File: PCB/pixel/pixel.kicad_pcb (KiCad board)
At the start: 2 copper layers, 75 x 75 mm, 281 parts, among them CON1 BARREL_JACK, P1 CONN_01X04, U1 APA102, U10 APA102, U100 APA102, U101 APA102, U102 APA102, U103 APA102, U104 APA102, U105 APA102, U106 APA102, U107 APA102, U108 APA102, U109 APA102, U11 APA102, U110 APA102, U111 APA102, U112 APA102, U113 APA102, U114 APA102, U115 APA102, U116 APA102, U117 APA102, U118 APA102, U119 APA102, U12 APA102, U120 APA102, U121 APA102, U122 APA102, U123 APA102, U124 APA102, U125 APA102, U126 APA102, U127 APA102, U128 APA102, U129 APA102, U13 APA102, U130 APA102, U131 APA102, U132 APA102, U133 APA102, U134 APA102, U135 APA102, U136 APA102, U137 APA102, U138 APA102, U139 APA102, U14 APA102, U140 APA102, U141 APA102, U142 APA102, U143 APA102, U144 APA102, U145 APA102, U146 APA102, U147 APA102, U148 APA102, U149 APA102, U15 APA102, U150 APA102, U151 APA102, U152 APA102, U153 APA102, U154 APA102, U155 APA102, U156 APA102, U157 APA102, U158 APA102, U159 APA102, U16 APA102, U160 APA102, U161 APA102, U162 APA102, U163 APA102, U164 APA102, U165 APA102, U166 APA102, U167 APA102, U168 APA102, U169 APA102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

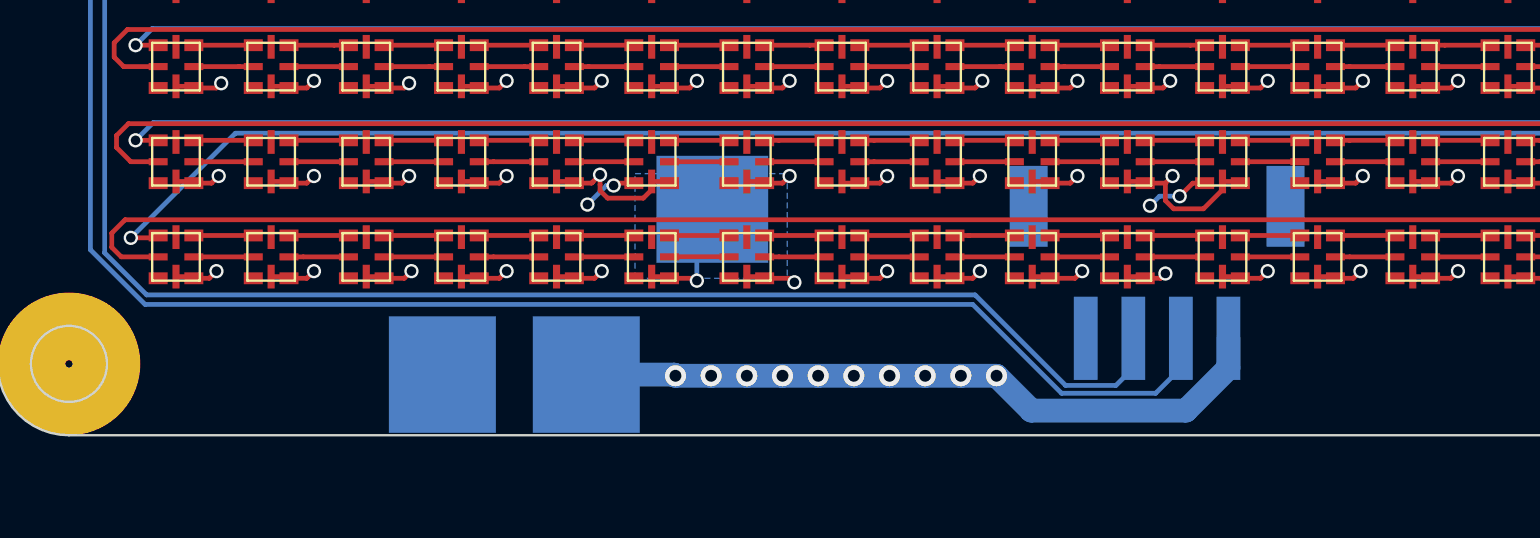
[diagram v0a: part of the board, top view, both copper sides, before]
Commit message: added fuse, fixed traces
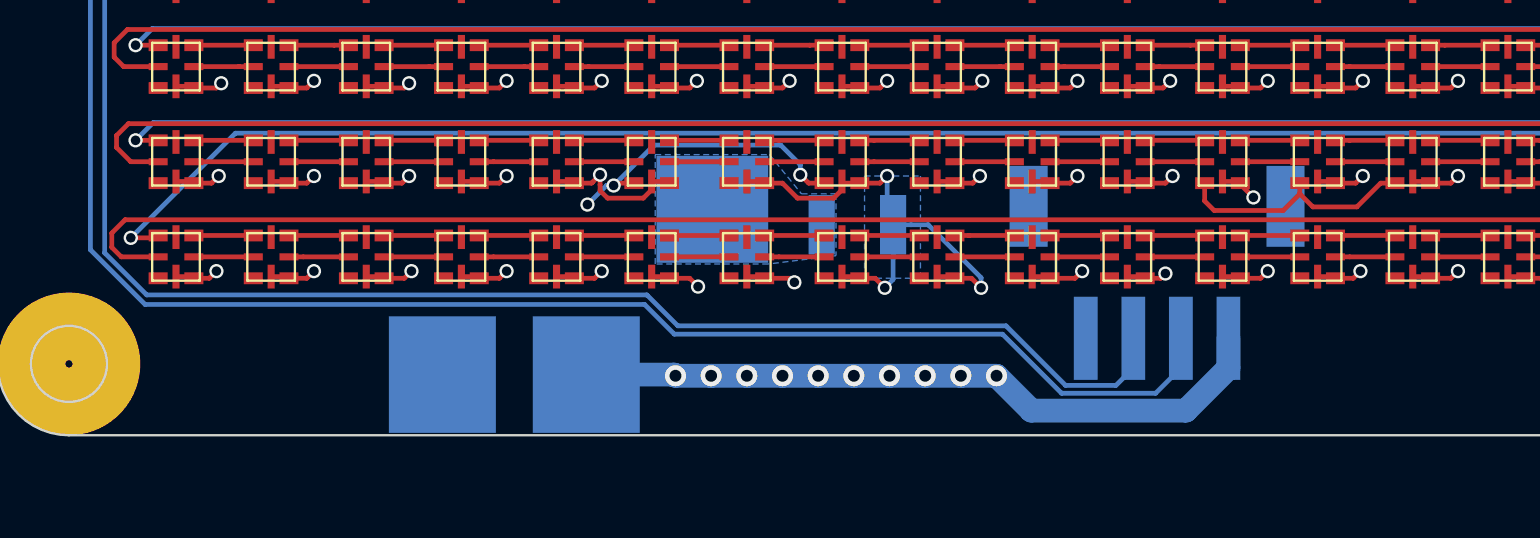
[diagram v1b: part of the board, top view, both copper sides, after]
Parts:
- added F1: 5A_Hold, idlehands_footprints:Fuse_SMD1210_Reflow, B.Cu at (133.2, 163.2)
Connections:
- CON1 pad 1: +5V -> Net-(CON1-Pad1)
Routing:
- net GND: track 123.9 -> 142.0 mm, vias 45 -> 44
- net +5V: track 531.4 -> 538.2 mm
- added copper zone on B.Cu, net Net-(CON1-Pad1)

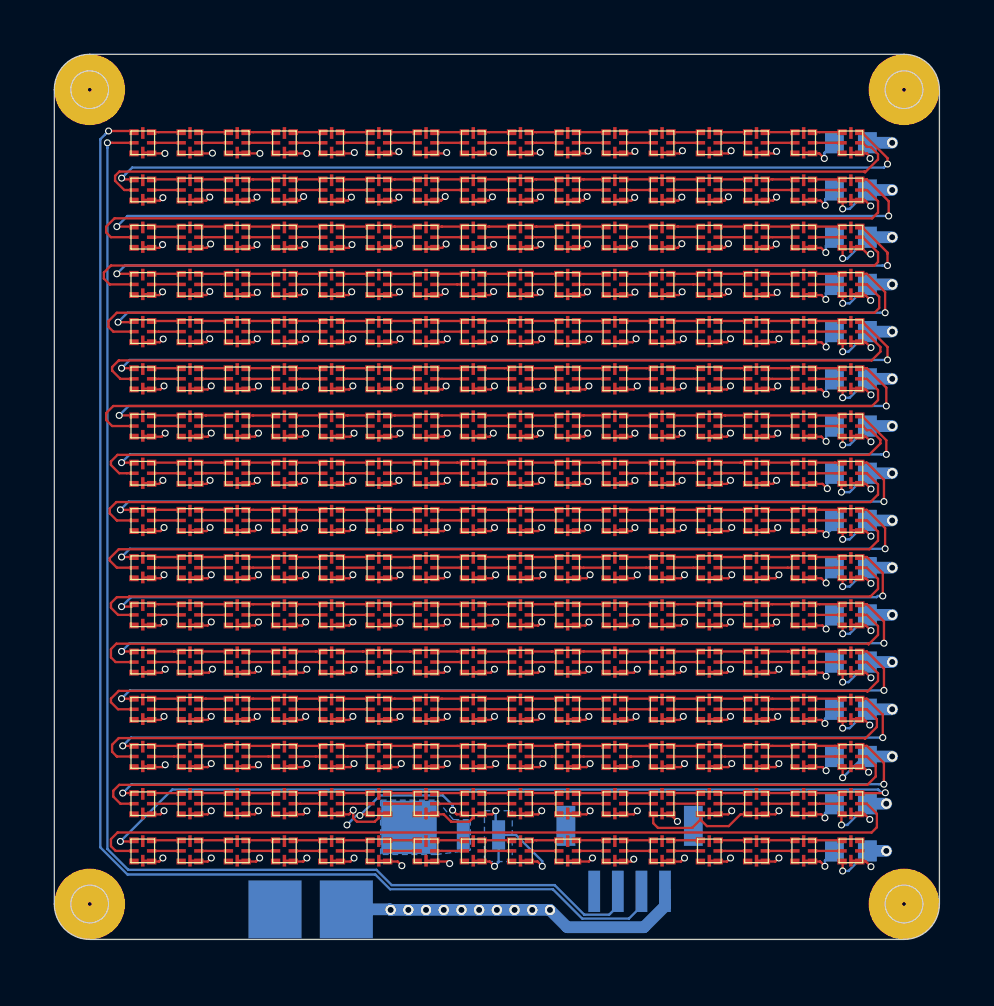
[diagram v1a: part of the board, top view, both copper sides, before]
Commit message: changed led pad layout
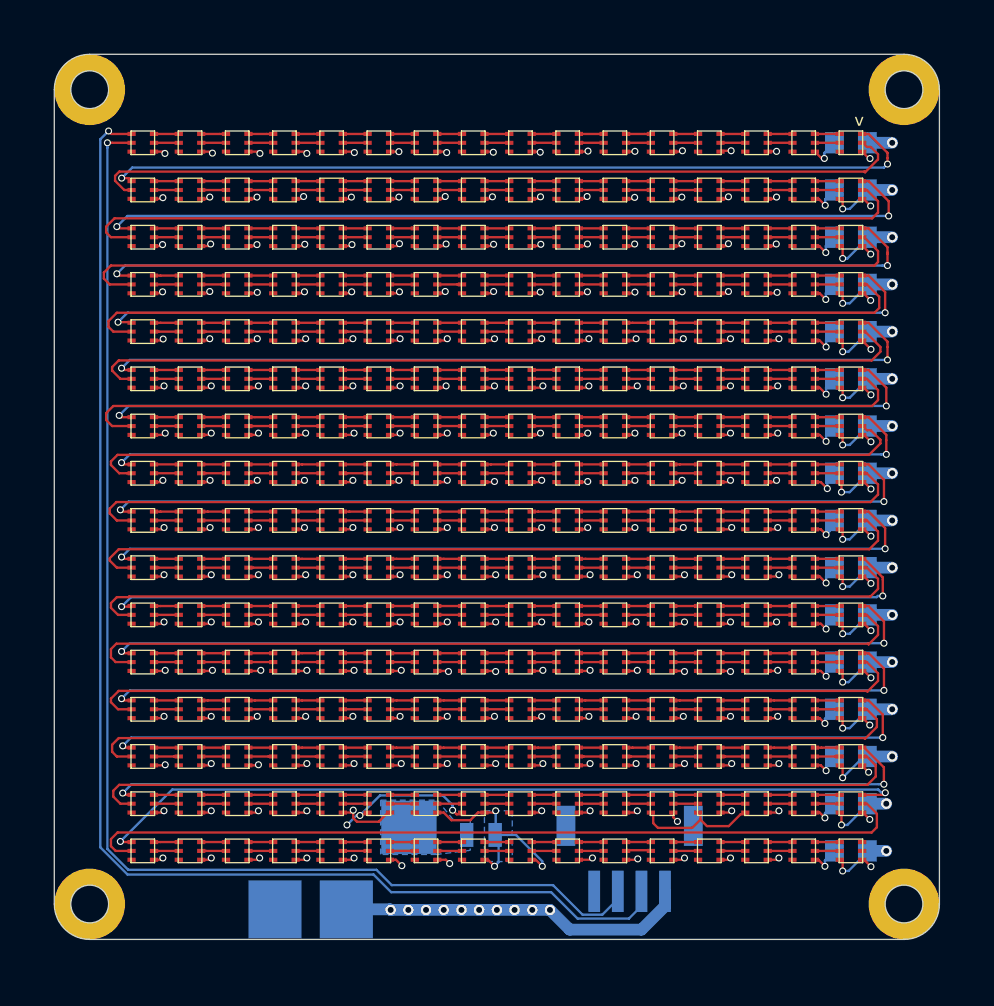
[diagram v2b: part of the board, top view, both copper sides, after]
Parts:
- F1: footprint idlehands_footprints:Fuse_SMD1210_Reflow -> Fuse_Holders_and_Fuses:Fuse_SMD1206_Reflow
- U1, U10, U100, U101, U102, U103, U104, U105, U106, U107, U108, U109, U11, U110, U111, U112, U113, U114, U115, U116, U117, U118, U119, U12, U120, U121, U122, U123, U124, U125, U126, U127, U128, U129, U13, U130, U131, U132, U133, U134, U135, U136, U137, U138, U139, U14, U140, U141, U142, U143, U144, U145, U146, U147, U148, U149, U15, U150, U151, U152, U153, U154, U155, U156, U157, U158, U159, U16, U160, U161, U162, U163, U164, U165, U166, U167, U168, U169, U17, U170, U171, U172, U173, U174, U175, U176, U177, U178, U179, U18, U180, U181, U182, U183, U184, U185, U186, U187, U188, U189, U19, U190, U191, U192, U193, U194, U195, U196, U197, U198, U199, U2, U20, U200, U201, U202, U203, U204, U205, U206, U207, U208, U209, U21, U210, U211, U212, U213, U214, U215, U216, U217, U218, U219, U22, U220, U221, U222, U223, U224, U225, U226, U227, U228, U229, U23, U230, U231, U232, U233, U234, U235, U236, U237, U238, U239, U24, U240, U241, U242, U243, U244, U245, U246, U247, U248, U249, U25, U250, U251, U252, U253, U254, U255, U256, U26, U27, U28, U29, U3, U30, U31, U32, U33, U34, U35, U36, U37, U38, U39, U4, U40, U41, U42, U43, U44, U45, U46, U47, U48, U49, U5, U50, U51, U52, U53, U54, U55, U56, U57, U58, U59, U6, U60, U61, U62, U63, U64, U65, U66, U67, U68, U69, U7, U70, U71, U72, U73, U74, U75, U76, U77, U78, U79, U8, U80, U81, U82, U83, U84, U85, U86, U87, U88, U89, U9, U90, U91, U92, U93, U94, U95, U96, U97, U98, U99: footprint idlehands_footprints:APA102-2020_NOGND -> idlehands_footprints:APA102-2020_AFSTYLE
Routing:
- net +5V: track 538.2 -> 278.6 mm
- net SD10: track 70.5 -> 69.7 mm
- net SD14: track 70.2 -> 69.6 mm
- net Net-(U228-Pad3): track 2.65 -> 2.10 mm
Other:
- rule trace_min: 0.1 -> 0.2
- board text added: "V0.2"
- board text added: "v"
